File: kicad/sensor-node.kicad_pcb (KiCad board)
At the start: 2 copper layers, 30 x 54 mm, 27 parts

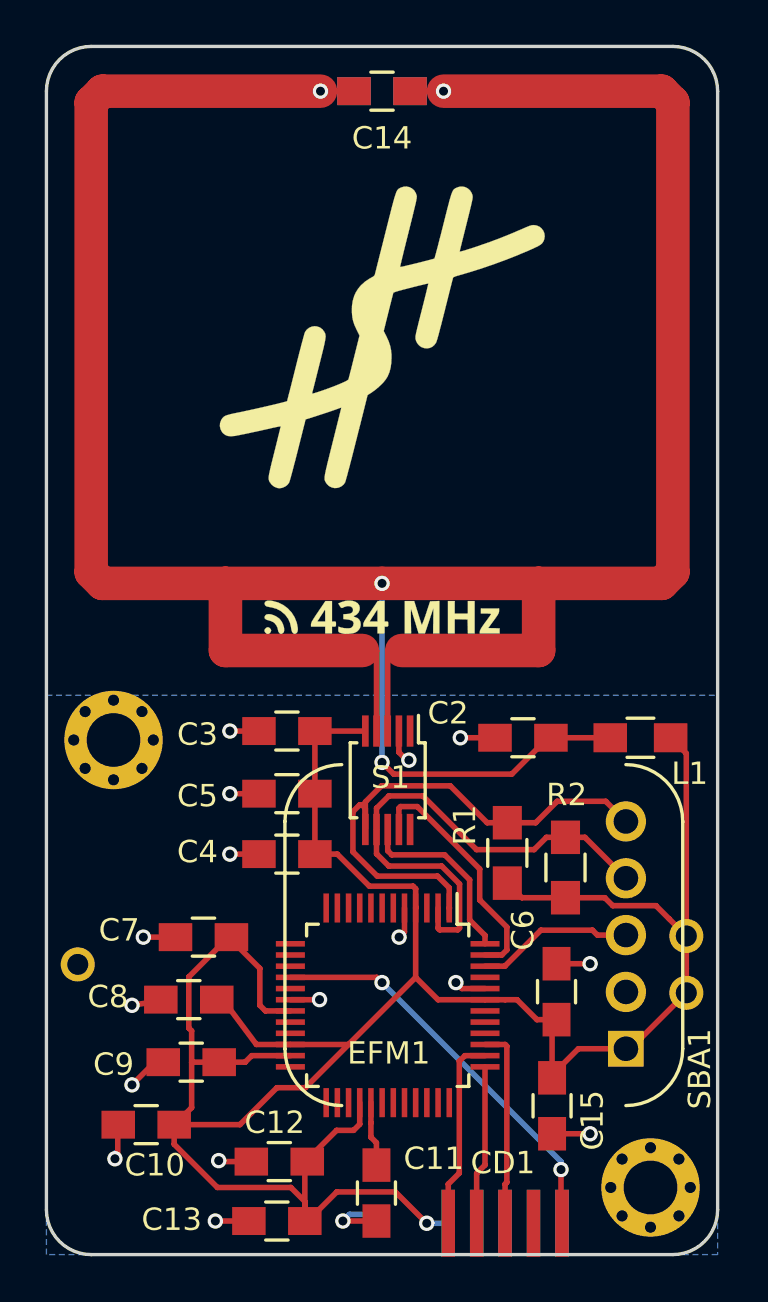
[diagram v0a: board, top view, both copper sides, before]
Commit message: fixed Si7012 pin assignment
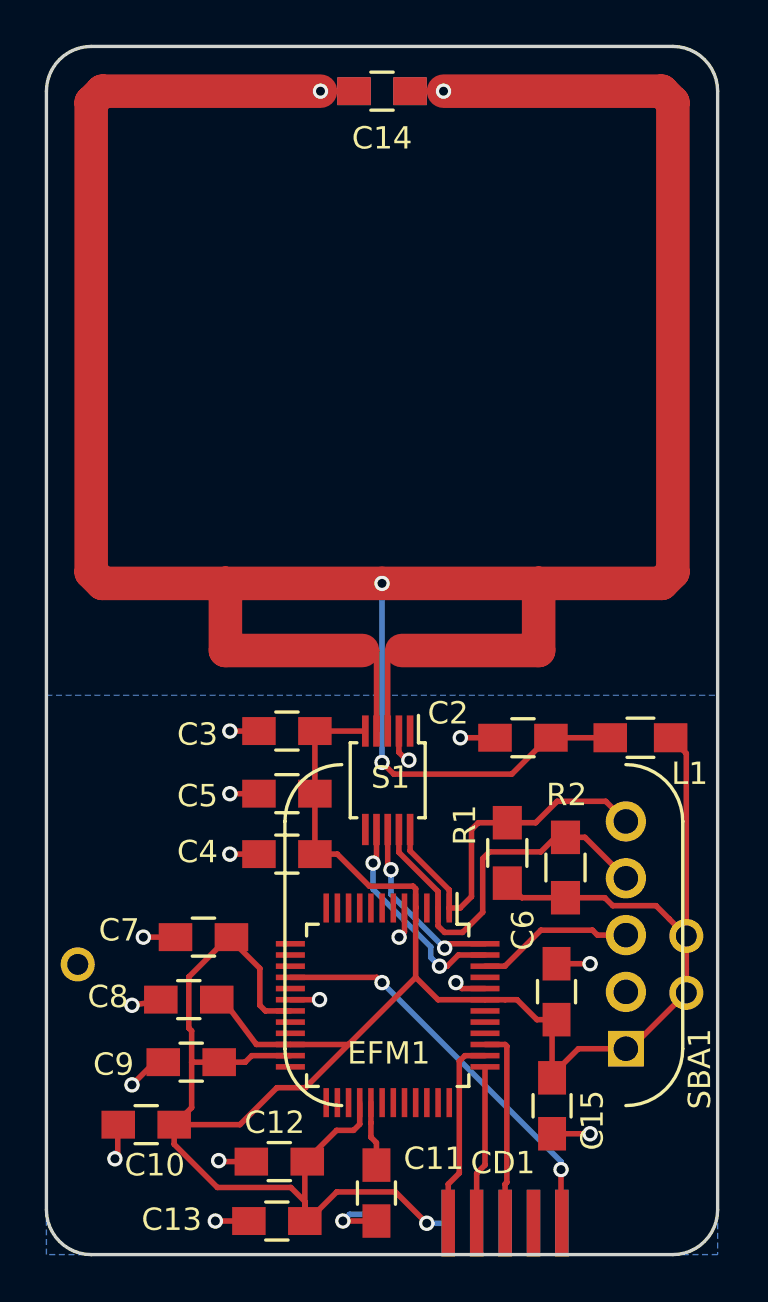
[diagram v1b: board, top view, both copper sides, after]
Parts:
- removed G***: LOGO, sensor-node-main:logo
- removed G***: LOGO, sensor-node-main:frequ
- removed REF** (x2): mounting, sensor-node:mounting
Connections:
- S1 pad 10: (no net) -> /SDA
- S1 pad 6: /SDA -> (no net)
- S1 pad 7: /SCL -> /RAD_INT
- S1 pad 9: /RAD_INT -> /SCL
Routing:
- net /SDA: track 25.4 -> 17.6 mm
- net /SCL: track 23.6 -> 17.5 mm
- net /RAD_INT: track 10.9 -> 9.65 mm, vias 0 -> 2
- net /RAD_ENABLE: track 8.30 -> 8.24 mm, vias 0 -> 2

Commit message: minor fix of the board
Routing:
- net GND: track 26.7 -> 27.5 mm
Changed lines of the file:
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@@
   (general
     (links 65)
-    (no_connects 1)
-    (area 137.070999 57.395999 167.221001 111.546001)
+    (no_connects 0)
+    (area 124.24918 56.4436 179.995999 119.171001)
     (thickness 0.8128)
     (drawings 12)
@@
   (segment (start 150.65 102.08) (end 148.05 102.08) (width 0.25) (layer F.Cu) (net 1))
   (segment (start 153.65 99.08) (end 150.65 102.08) (width 0.25) (layer F.Cu) (net 1))
+  (segment (start 156.75 99.58) (end 157.637 99.58) (width 0.25) (layer F.Cu) (net 2))
+  (segment (start 157.637 99.58) (end 158.246 98.971) (width 0.25) (layer F.Cu) (net 2))
+  (via (at 158.246 98.971) (size 0.69) (drill 0.4) (layers F.Cu B.Cu) (net 2))
+  (segment (start 153.15 95.98) (end 153.15 96.867) (width 0.25) (layer F.Cu) (net 2))
+  (segment (start 153.15 96.867) (end 152.446 97.571) (width 0.25) (layer F.Cu) (net 2))
+  (via (at 152.446 97.571) (size 0.69) (drill 0.4) (layers F.Cu B.Cu) (net 2))
   (segment (start 146.196 109.971) (end 144.696 109.971) (width 0.25) (layer F.Cu) (net 2))
   (via (at 144.696 109.971) (size 0.69) (drill 0.4) (layers F.Cu B.Cu) (net 2))
@@
   (via (at 140.208 107.188) (size 0.69) (drill 0.4) (layers F.Cu B.Cu) (net 2) (status 30))
   (via (at 140.97 103.886) (size 0.69) (drill 0.4) (layers F.Cu B.Cu) (net 2))
-  (via (at 152.908 97.282) (size 0.69) (drill 0.4) (layers F.Cu B.Cu) (net 2))
-  (via (at 155.448 99.314) (size 0.69) (drill 0.4) (layers F.Cu B.Cu) (net 2))
   (via (at 140.97 100.33) (size 0.69) (drill 0.4) (layers F.Cu B.Cu) (net 2))
   (via (at 149.352 100.076) (size 0.69) (drill 0.4) (layers F.Cu B.Cu) (net 2))
@@
   (segment (start 140.208 106.934) (end 140.208 107.188) (width 0.25) (layer B.Cu) (net 2))
   (segment (start 149.348 100.08) (end 149.352 100.076) (width 0.25) (layer F.Cu) (net 2))
-  (segment (start 153.15 95.98) (end 153.15 97.04) (width 0.25) (layer F.Cu) (net 2))
-  (segment (start 155.714 99.58) (end 155.448 99.314) (width 0.25) (layer F.Cu) (net 2))
   (segment (start 142.514 100.076) (end 140.97 100.33) (width 0.25) (layer F.Cu) (net 2) (status 10))
   (segment (start 140.335 107.061) (end 140.208 107.188) (width 0.25) (layer F.Cu) (net 2))
   (segment (start 140.335 105.664) (end 140.335 107.061) (width 0.25) (layer F.Cu) (net 2))
-  (segment (start 156.75 99.58) (end 155.714 99.58) (width 0.25) (layer F.Cu) (net 2))
   (segment (start 148.05 100.08) (end 149.348 100.08) (width 0.25) (layer F.Cu) (net 2))
   (segment (start 142.875 97.282) (end 141.478 97.282) (width 0.25) (layer F.Cu) (net 2))
-  (segment (start 153.15 97.04) (end 152.908 97.282) (width 0.25) (layer F.Cu) (net 2))
   (segment (start 142.367 102.87) (end 141.986 102.87) (width 0.25) (layer F.Cu) (net 2))
   (segment (start 141.986 102.87) (end 140.97 103.886) (width 0.25) (layer F.Cu) (net 2))

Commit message: increased version number of the board
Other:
- board text added: "www.hochreiner.net sensor node V1.0.1"
- board text removed: "www.hochreiner.net sensor node V1.0.0"
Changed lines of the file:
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@@
   )
   (setup
-    (last_trace_width 0.25)
+    (last_trace_width 0.1524)
     (user_trace_width 0.25)
     (trace_clearance 0.1524)
@@
     )
   )
-  (gr_text "www.hochreiner.net\nsensor node\nV1.0.0" (at 152.096 70.471) (layer B.SilkS)
+  (gr_text "www.hochreiner.net\nsensor node\nV1.0.1" (at 152.096 70.471) (layer B.SilkS)
     (effects (font (size 1.5 1.5) (thickness 0.3)) (justify mirror))
   )

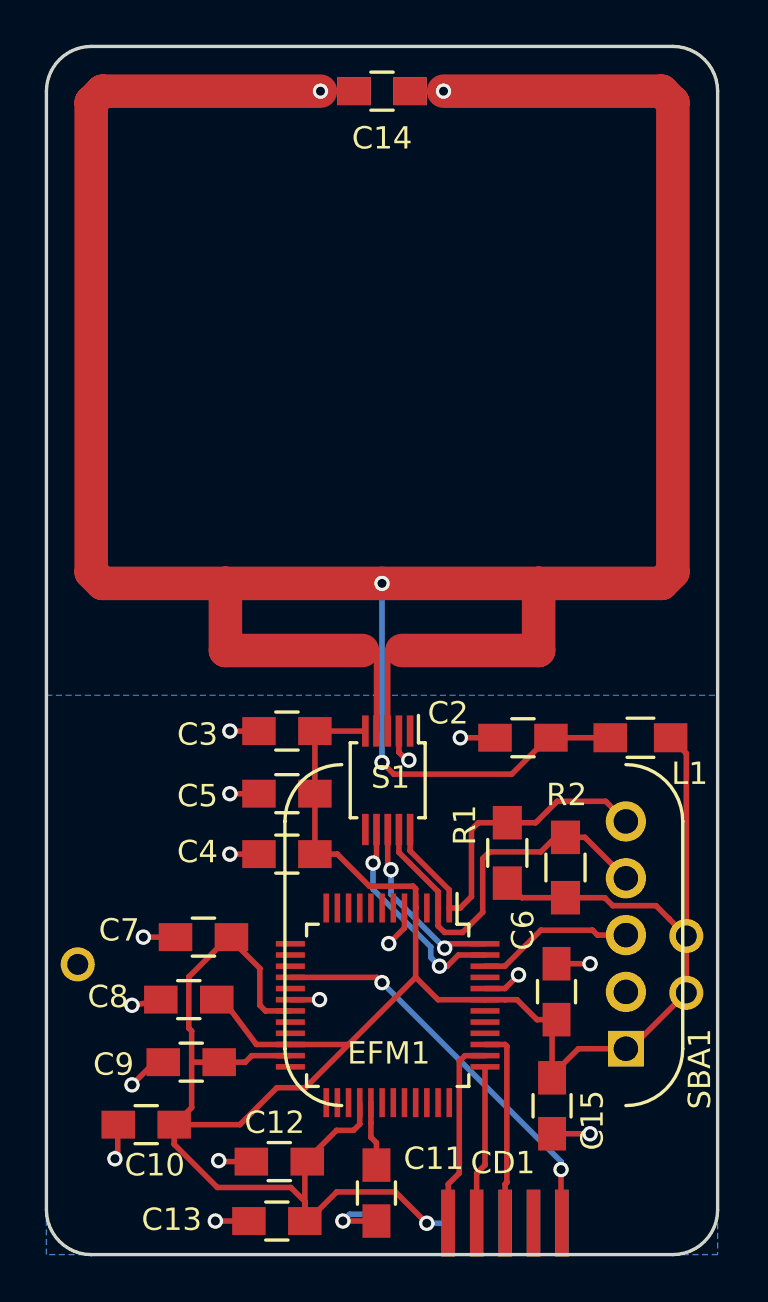
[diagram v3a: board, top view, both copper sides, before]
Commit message: added logo, mounting, and stitching vias
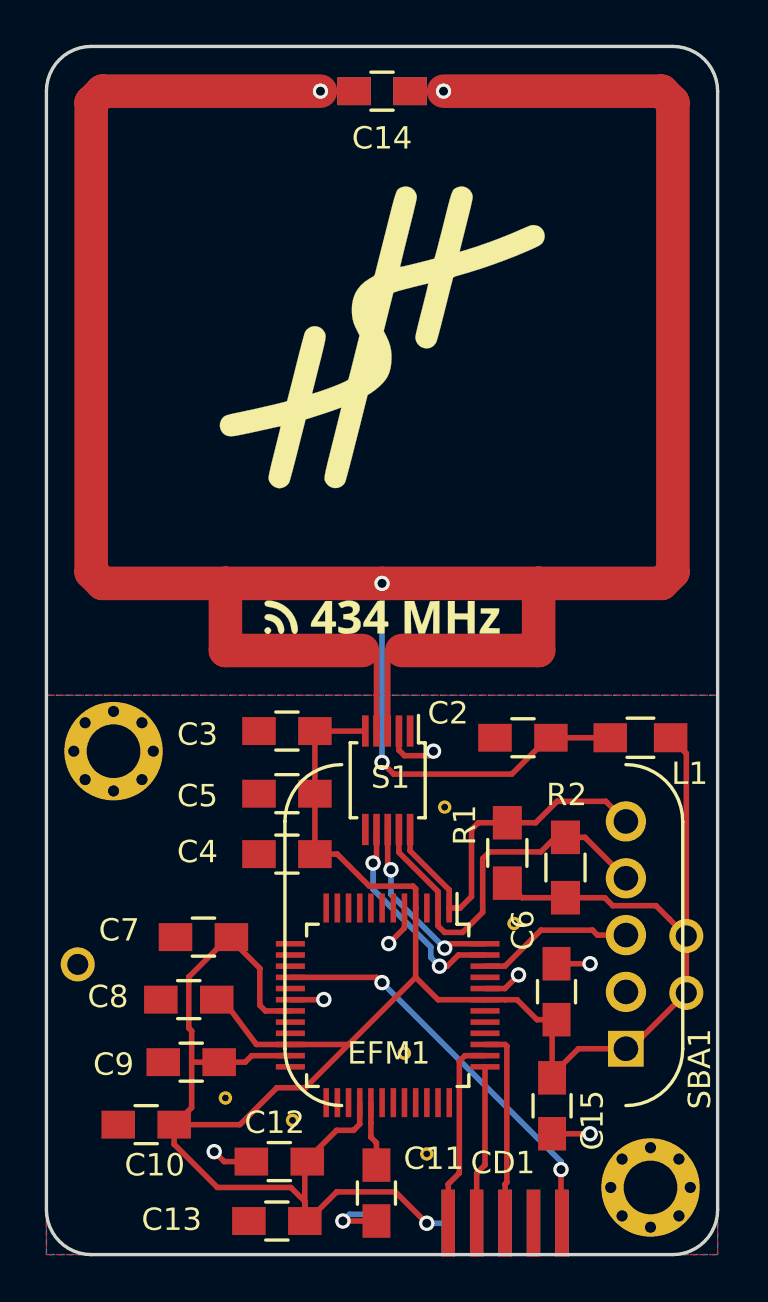
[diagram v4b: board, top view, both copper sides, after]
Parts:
- added G***: LOGO, sensor-node-main:frequ, F.Cu at (152.1, 83.0)
- added G***: LOGO, sensor-node-main:logo, F.Cu at (152.1, 70.5)
- added REF**: via-0.6mm, sensor-node:via-0.6mm, F.Cu at (158.0, 96.7)
- added REF**: via-0.6mm, sensor-node:via-0.6mm, F.Cu at (154.9, 91.5)
- added REF**: via-0.6mm, sensor-node:via-0.6mm, F.Cu at (154.1, 107.0)
- added REF**: via-0.6mm, sensor-node:via-0.6mm, F.Cu at (145.1, 104.5)
- added REF**: via-0.6mm, sensor-node:via-0.6mm, F.Cu at (148.1, 105.5)
- added REF**: mounting, sensor-node:mounting, F.Cu at (140.1, 89.0)
- added REF**: mounting, sensor-node:mounting, F.Cu at (164.1, 108.5)
- added REF**: via-0.6mm, sensor-node:via-0.6mm, F.Cu at (153.1, 102.5)
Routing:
- net GND: track 27.5 -> 16.0 mm, vias 17 -> 8
- added copper zone on F.Cu, net GND

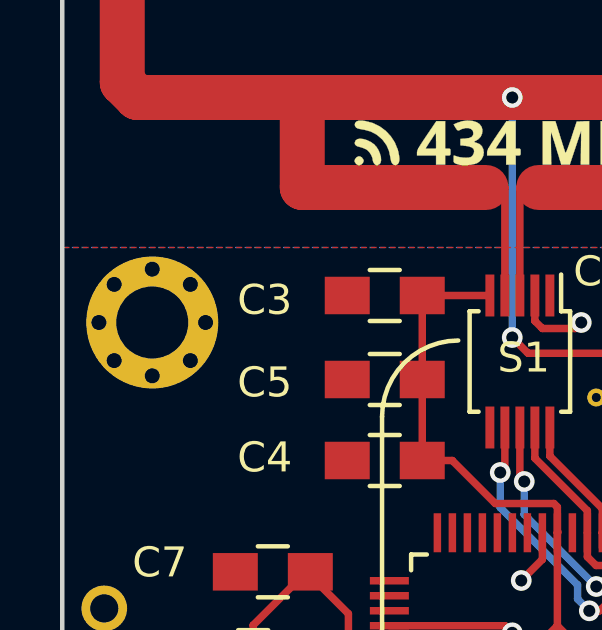
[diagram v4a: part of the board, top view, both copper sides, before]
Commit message: returned mounting hole to former position
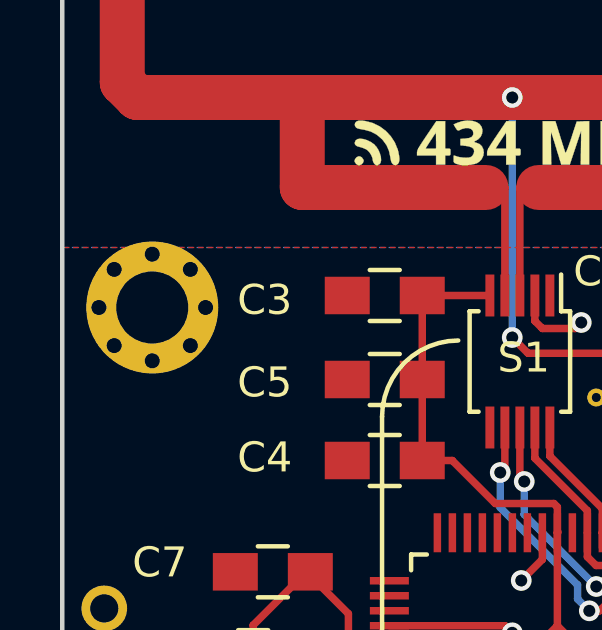
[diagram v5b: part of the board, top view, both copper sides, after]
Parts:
- moved REF** 0.50 mm to (140.1, 88.5)
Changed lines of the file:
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@@
 (kicad_pcb (version 4) (host pcbnew 4.0.6)
   (general
-    (links 0)
+    (links 89)
     (no_connects 0)
     (area 137.070999 57.395999 167.221001 111.546001)
@@
   )
   (setup
-    (last_trace_width 0.25)
+    (last_trace_width 0.1524)
     (user_trace_width 0.25)
     (trace_clearance 0.1524)
@@
   )
   (module sensor-node:mounting (layer F.Cu)
-    (at 140.146 88.971)
+    (at 140.146 88.471)
     (zone_connect 2)
     (fp_text reference REF** (at 0 0.5) (layer F.SilkS) hide
